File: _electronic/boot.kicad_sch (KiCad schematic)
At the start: 10 parts

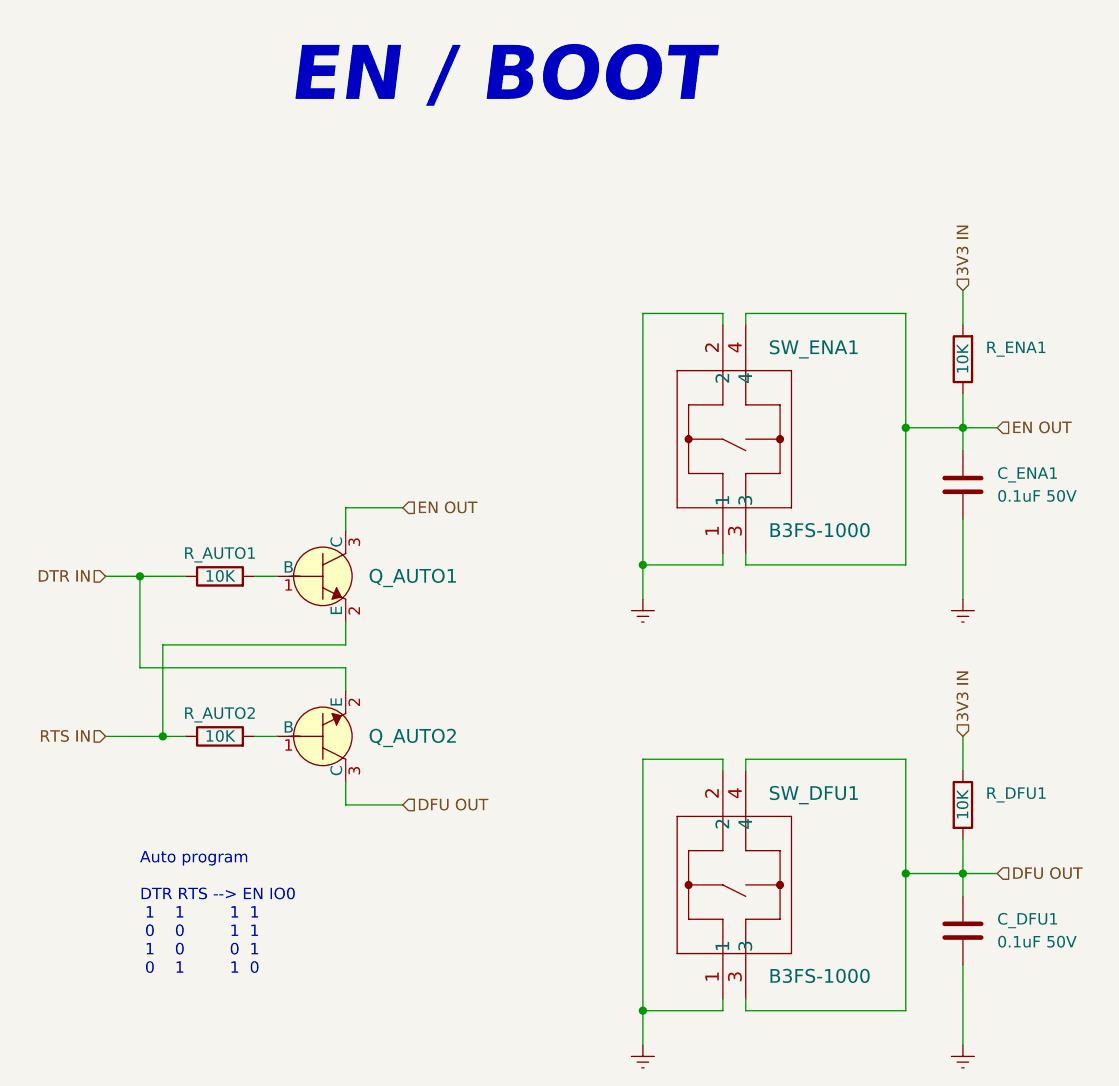
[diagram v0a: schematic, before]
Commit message: BETA first upload
nothing major done here:
* updated KiCAD files to v9
* removed alternative 6v feed-in. The proposed buck converter is fine.
* added to all components LCSC component IDs. With this, exporting the project as gerber files also automatically creates correct BOM for JLCPCB manufacturing
*
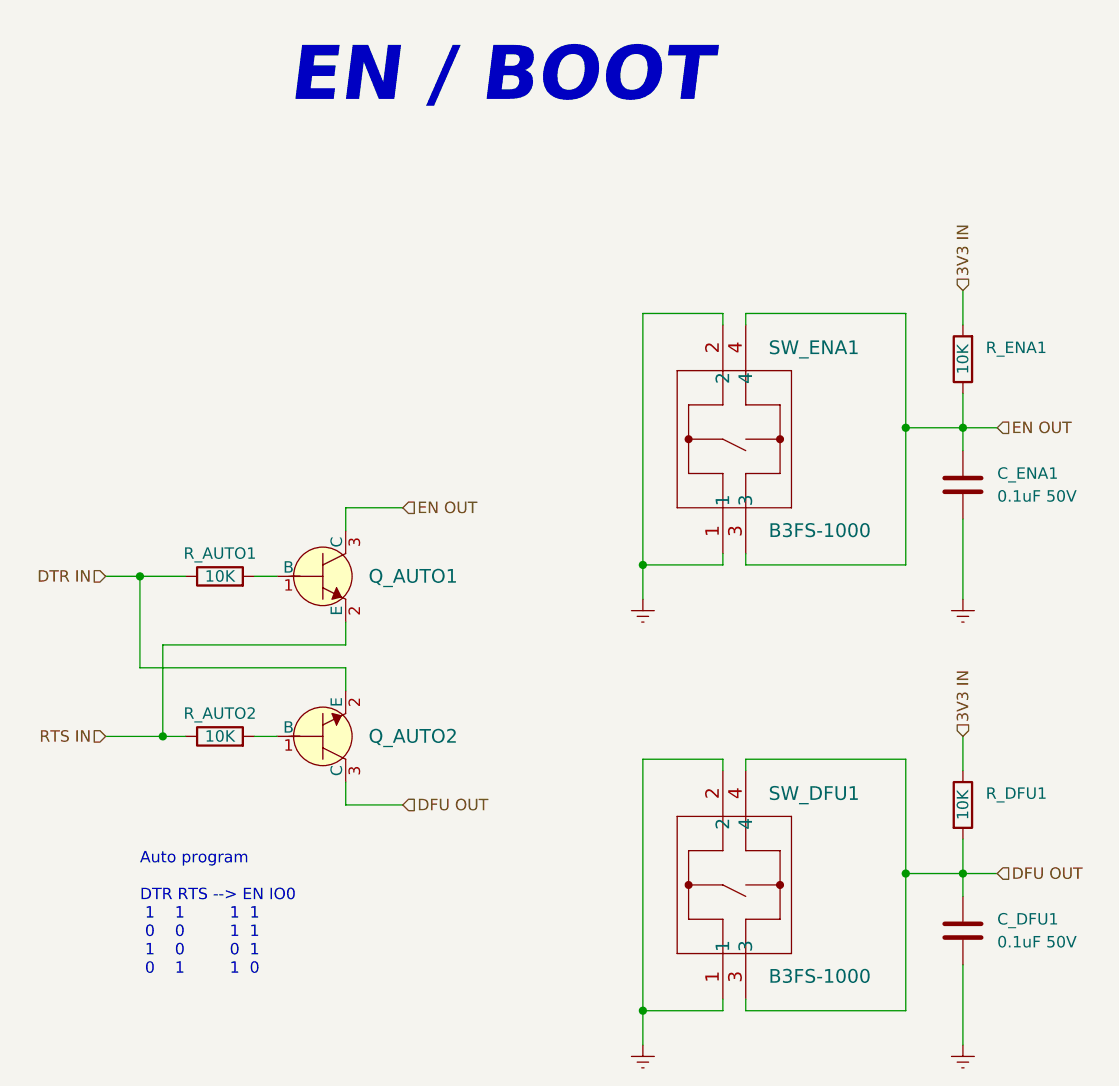
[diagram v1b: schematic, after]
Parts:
- C_DFU1, C_ENA1: LCSC (none) -> C14663
- Q_AUTO1, Q_AUTO2: LCSC (none) -> C2914407
- R_AUTO1, R_AUTO2, R_DFU1, R_ENA1: LCSC (none) -> C25804
- SW_DFU1, SW_ENA1: LCSC (none) -> C271750
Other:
- title: E-TKT v1.0 -> E-TKT v2.0 BETA

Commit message: Added CAD, cleaned up KiCAD some more
Added a FreeCAD Assembly. This will serve for minor updated to the printable parts.
Updated USB-C component to standard KiCAD libary-integrated version, because the pinout of the schematic symbol was messing with the pinout of the footprint
exported the PCB as step so it could be imported to FreeCAD
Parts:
- SW_DFU1, SW_ENA1: footprint b3fs:B3FS-1000 -> EASYEDA2KICAD:KEY-SMD_4P-L6.0-W6.3-P4.50-LS8.0
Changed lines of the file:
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@@
 			)
 		)
-		(property "Footprint" "b3fs:B3FS-1000"
+		(property "Footprint" "EASYEDA2KICAD:KEY-SMD_4P-L6.0-W6.3-P4.50-LS8.0"
 			(at 156.464 82.55 0)
 			(effects
@@
 			)
 		)
-		(property "Footprint" "b3fs:B3FS-1000"
+		(property "Footprint" "EASYEDA2KICAD:KEY-SMD_4P-L6.0-W6.3-P4.50-LS8.0"
 			(at 156.464 132.08 0)
 			(effects

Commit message: Minor adjustments of CAD and EDA
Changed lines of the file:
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@@
 		)
 		(property "Value" "10K"
-			(at 106.68 97.79 90)
+			(at 106.68 100.33 90)
 			(effects
 				(font
@@
 		)
 		(property "Value" "10K"
-			(at 106.68 115.57 90)
-			(effects
-				(font
+			(at 106.68 118.11 90)
+			(effects
+				(font

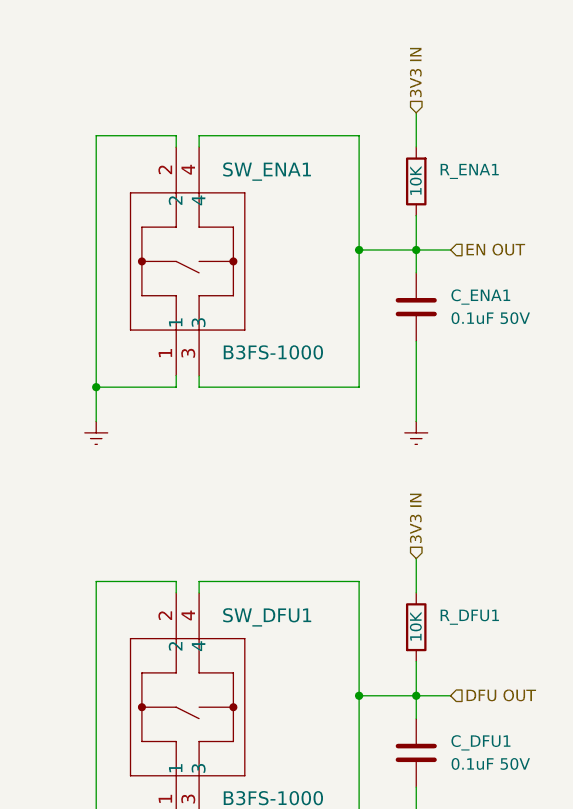
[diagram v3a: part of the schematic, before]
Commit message: Updated layout of schematic symbol's text
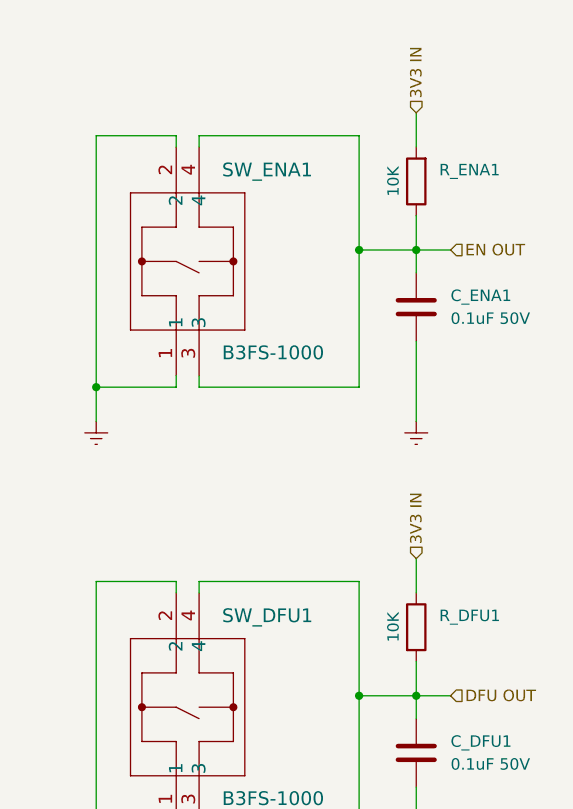
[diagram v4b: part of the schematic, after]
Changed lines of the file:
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@@
 		)
 		(property "Value" "10K"
-			(at 189.23 123.19 90)
+			(at 186.69 123.19 90)
 			(effects
 				(font
@@
 		)
 		(property "Value" "10K"
-			(at 189.23 73.66 90)
-			(effects
-				(font
+			(at 186.69 73.66 90)
+			(effects
+				(font
